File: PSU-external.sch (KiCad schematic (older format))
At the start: 40 parts, among them J3 IEC-C13-SOCKET, P18 CONN_1, P19 CONN_1, P20 CONN_1, P21 CONN_1, P22 CONN_1, T1 TRIAD-FS16-400-C2, T2 TRIAD-FS48-750-C2, U10 P0720ECL, U11 P0720ECL, U12 MC7805C, U13 LM7818CT, U14 LM7918CT

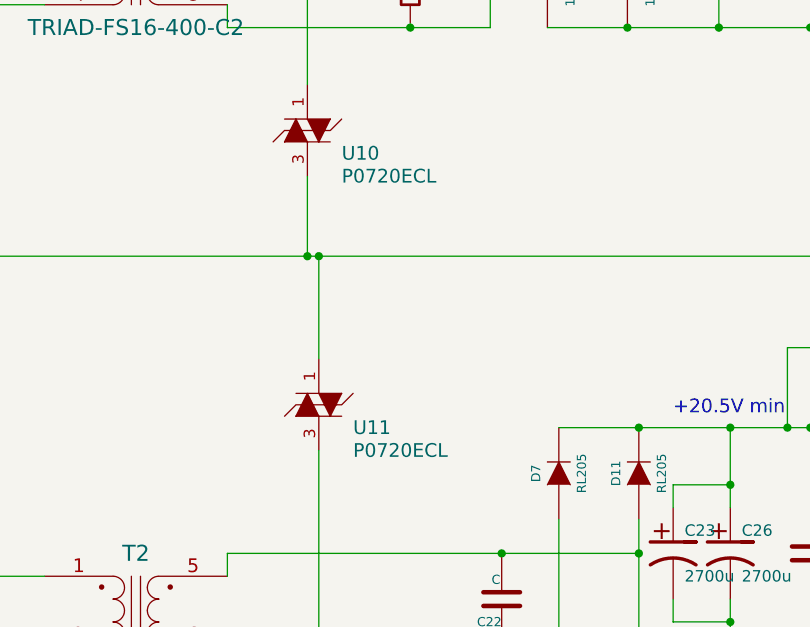
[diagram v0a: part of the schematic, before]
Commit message: Changed from the P0720ECL SIDACtor to the more sensitive P0300.
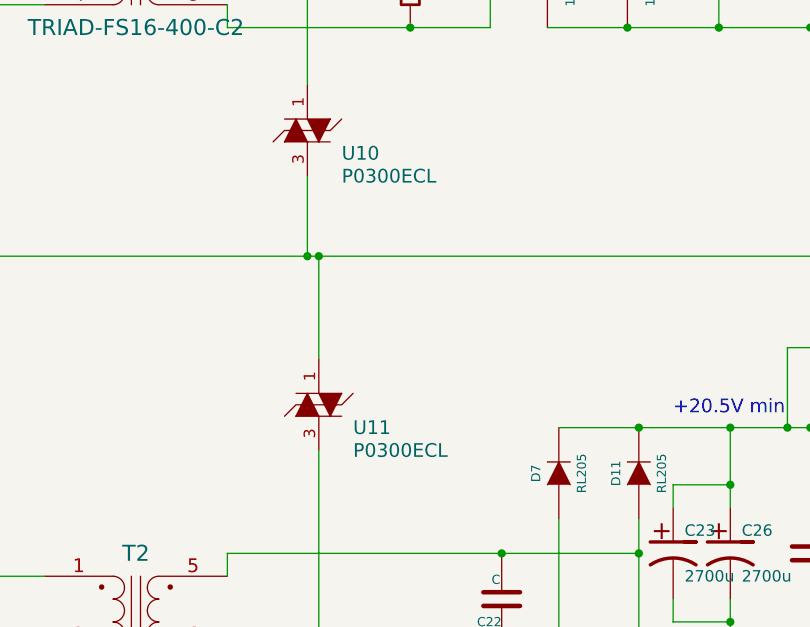
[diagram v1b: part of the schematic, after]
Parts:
- removed U10, U11: P0720ECL, symbol P0720ECL
- added U10, U11: P0300ECL, symbol P0300ECL
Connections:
- net AGND_EXT: now also U11.3
- net SAF_GND: now also U10.3, U11.1
- net at T1.6 (SB), T1.7 (SC): now also U10.1
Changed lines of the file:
@@
 Wire Wire Line
 	5400 3850 5400 4800
-$Comp
-L P0720ECL U10
-U 1 1 537CB1E3
-P 5350 2450
-F 0 "U10" H 5500 2350 60  0000 L CNN
-F 1 "P0720ECL" H 5500 2250 60  0000 L CNN
-F 2 "" H 5350 2500 60  0001 C CNN
-F 3 "~" H 5350 2500 60  0000 C CNN
-F 4 "F5278-ND" H 5350 2450 60  0001 C CNN "DigiKey"
-	1    5350 2450
-	1    0    0    -1
-$EndComp
 Wire Wire Line
 	6950 5050 6950 4950
@@
 	1    6750 1800
 	0    -1   -1   0
-$EndComp
-$Comp
-L P0720ECL U11
-U 1 1 537DAB3C
-P 5400 3650
-F 0 "U11" H 5550 3550 60  0000 L CNN
-F 1 "P0720ECL" H 5550 3450 60  0000 L CNN
-F 2 "" H 5400 3700 60  0001 C CNN
-F 3 "~" H 5400 3700 60  0000 C CNN
-F 4 "F5278-ND" H 5400 3650 60  0001 C CNN "DigiKey"
-	1    5400 3650
-	1    0    0    -1
 $EndComp
 $Comp
@@
 	2400 2900 2400 3000
 Connection ~ 2400 3000
+$Comp
+L P0300ECL U10
+U 1 1 5389743A
+P 5350 2450
+F 0 "U10" H 5500 2350 60  0000 L CNN
+F 1 "P0300ECL" H 5500 2250 60  0000 L CNN
+F 2 "" H 5350 2500 60  0000 C CNN
+F 3 "" H 5350 2500 60  0000 C CNN
+F 4 "P0300ECL-ND" H 5350 2450 60  0001 C CNN "DigiKey"
+	1    5350 2450
+	1    0    0    -1
+$EndComp
+$Comp
+L P0300ECL U11
+U 1 1 53897463
+P 5400 3650
+F 0 "U11" H 5550 3550 60  0000 L CNN
+F 1 "P0300ECL" H 5550 3450 60  0000 L CNN
+F 2 "" H 5400 3700 60  0000 C CNN
+F 3 "" H 5400 3700 60  0000 C CNN
+F 4 "P0300ECL-ND" H 5400 3650 60  0001 C CNN "DigiKey"
+	1    5400 3650
+	1    0    0    -1
+$EndComp
 $EndSCHEMATC

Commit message: Changed to use the fixed IEC socket device; the PSU netlist should now be (more) correct.
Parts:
- C21, C22: footprint (none) -> Capacitors_ThroughHole:Capacitor12MMDiscRM7.75
- F1, J3: footprint (none) -> Oddities:Dummy_Empty
- P18, P19, P20, P21, P22: footprint (none) -> Connect:1pin
- R21, R22: footprint (none) -> Resistors_ThroughHole:Resistor_Horizontal_RM15mm
- U10, U11: footprint (none) -> Housings_TO-92:TO-92-Free-inline-wide
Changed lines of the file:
@@
 F 0 "C22" H 6200 4600 40  0000 L CNN
 F 1 "C" H 6206 4415 40  0000 L CNN
-F 2 "" H 6238 4350 30  0001 C CNN
+F 2 "Capacitors_ThroughHole:Capacitor12MMDiscRM7.75" H 6238 4350 30  0001 C CNN
 F 3 "~" H 6200 4500 60  0000 C CNN
 	1    6200 4500
@@
 F 0 "R22" V 6280 5100 40  0000 C CNN
 F 1 "R" V 6207 5101 40  0000 C CNN
-F 2 "" V 6130 5100 30  0001 C CNN
+F 2 "Resistors_ThroughHole:Resistor_Horizontal_RM15mm" V 6130 5100 30  0001 C CNN
 F 3 "~" H 6200 5100 30  0000 C CNN
 	1    6200 5100
@@
 F 0 "C21" H 5800 1300 40  0000 L CNN
 F 1 "C" H 5806 1115 40  0000 L CNN
-F 2 "" H 5838 1050 30  0001 C CNN
+F 2 "Capacitors_ThroughHole:Capacitor12MMDiscRM7.75" H 5838 1050 30  0001 C CNN
 F 3 "~" H 5800 1200 60  0000 C CNN
 	1    5800 1200
@@
 F 0 "R21" V 5880 1750 40  0000 C CNN
 F 1 "R" V 5807 1751 40  0000 C CNN
-F 2 "" V 5730 1750 30  0001 C CNN
+F 2 "Resistors_ThroughHole:Resistor_Horizontal_RM15mm" V 5730 1750 30  0001 C CNN
 F 3 "~" H 5800 1750 30  0000 C CNN
 	1    5800 1750
@@
 F 0 "J3" H 1800 3000 60  0000 L CNN
 F 1 "IEC-C13-SOCKET" H 1800 2900 60  0000 L CNN
-F 2 "" H 2000 4100 60  0001 C CNN
+F 2 "Oddities:Dummy_Empty" H 2000 4100 60  0001 C CNN
 F 3 "~" H 2000 4100 60  0000 C CNN
 F 4 "CCM1724-ND" H 2050 3700 60  0001 C CNN "DigiKey"
@@
 F 0 "F1" H 2650 5050 40  0000 C CNN
 F 1 "FUSE" H 2450 4950 40  0000 C CNN
-F 2 "" H 2550 5000 60  0001 C CNN
+F 2 "Oddities:Dummy_Empty" H 2550 5000 60  0001 C CNN
 F 3 "~" H 2550 5000 60  0000 C CNN
 F 4 "F1764-ND" H 2550 5000 60  0001 C CNN "DigiKey"
@@
 F 0 "P22" H 3080 3700 40  0000 L CNN
 F 1 "CONN_1" H 3000 3755 30  0001 C CNN
-F 2 "" H 3000 3700 60  0000 C CNN
+F 2 "Connect:1pin" H 3000 3700 60  0001 C CNN
 F 3 "" H 3000 3700 60  0000 C CNN
 	1    3000 3700
@@
 F 0 "P21" H 2930 3700 40  0000 L CNN
 F 1 "CONN_1" H 2850 3755 30  0001 C CNN
-F 2 "" H 2850 3700 60  0000 C CNN
+F 2 "Connect:1pin" H 2850 3700 60  0001 C CNN
 F 3 "" H 2850 3700 60  0000 C CNN
 	1    2850 3700
@@
 F 0 "P20" H 2780 3700 40  0000 L CNN
 F 1 "CONN_1" H 2700 3755 30  0001 C CNN
-F 2 "" H 2700 3700 60  0000 C CNN
+F 2 "Connect:1pin" H 2700 3700 60  0001 C CNN
 F 3 "" H 2700 3700 60  0000 C CNN
 	1    2700 3700
@@
 F 0 "P19" H 2630 3700 40  0000 L CNN
 F 1 "CONN_1" H 2550 3755 30  0001 C CNN
-F 2 "" H 2550 3700 60  0000 C CNN
+F 2 "Connect:1pin" H 2550 3700 60  0001 C CNN
 F 3 "" H 2550 3700 60  0000 C CNN
 	1    2550 3700
@@
 F 0 "P18" H 2480 2750 40  0000 L CNN
 F 1 "CONN_1" H 2400 2805 30  0001 C CNN
-F 2 "" H 2400 2750 60  0000 C CNN
+F 2 "Connect:1pin" H 2400 2750 60  0001 C CNN
 F 3 "" H 2400 2750 60  0000 C CNN
 	1    2400 2750
@@
 F 0 "U10" H 5500 2350 60  0000 L CNN
 F 1 "P0300ECL" H 5500 2250 60  0000 L CNN
-F 2 "" H 5350 2500 60  0000 C CNN
+F 2 "Housings_TO-92:TO-92-Free-inline-wide" H 5350 2500 60  0001 C CNN
 F 3 "" H 5350 2500 60  0000 C CNN
 F 4 "P0300ECL-ND" H 5350 2450 60  0001 C CNN "DigiKey"
@@
 F 0 "U11" H 5550 3550 60  0000 L CNN
 F 1 "P0300ECL" H 5550 3450 60  0000 L CNN
-F 2 "" H 5400 3700 60  0000 C CNN
+F 2 "Housings_TO-92:TO-92-Free-inline-wide" H 5400 3700 60  0001 C CNN
 F 3 "" H 5400 3700 60  0000 C CNN
 F 4 "P0300ECL-ND" H 5400 3650 60  0001 C CNN "DigiKey"

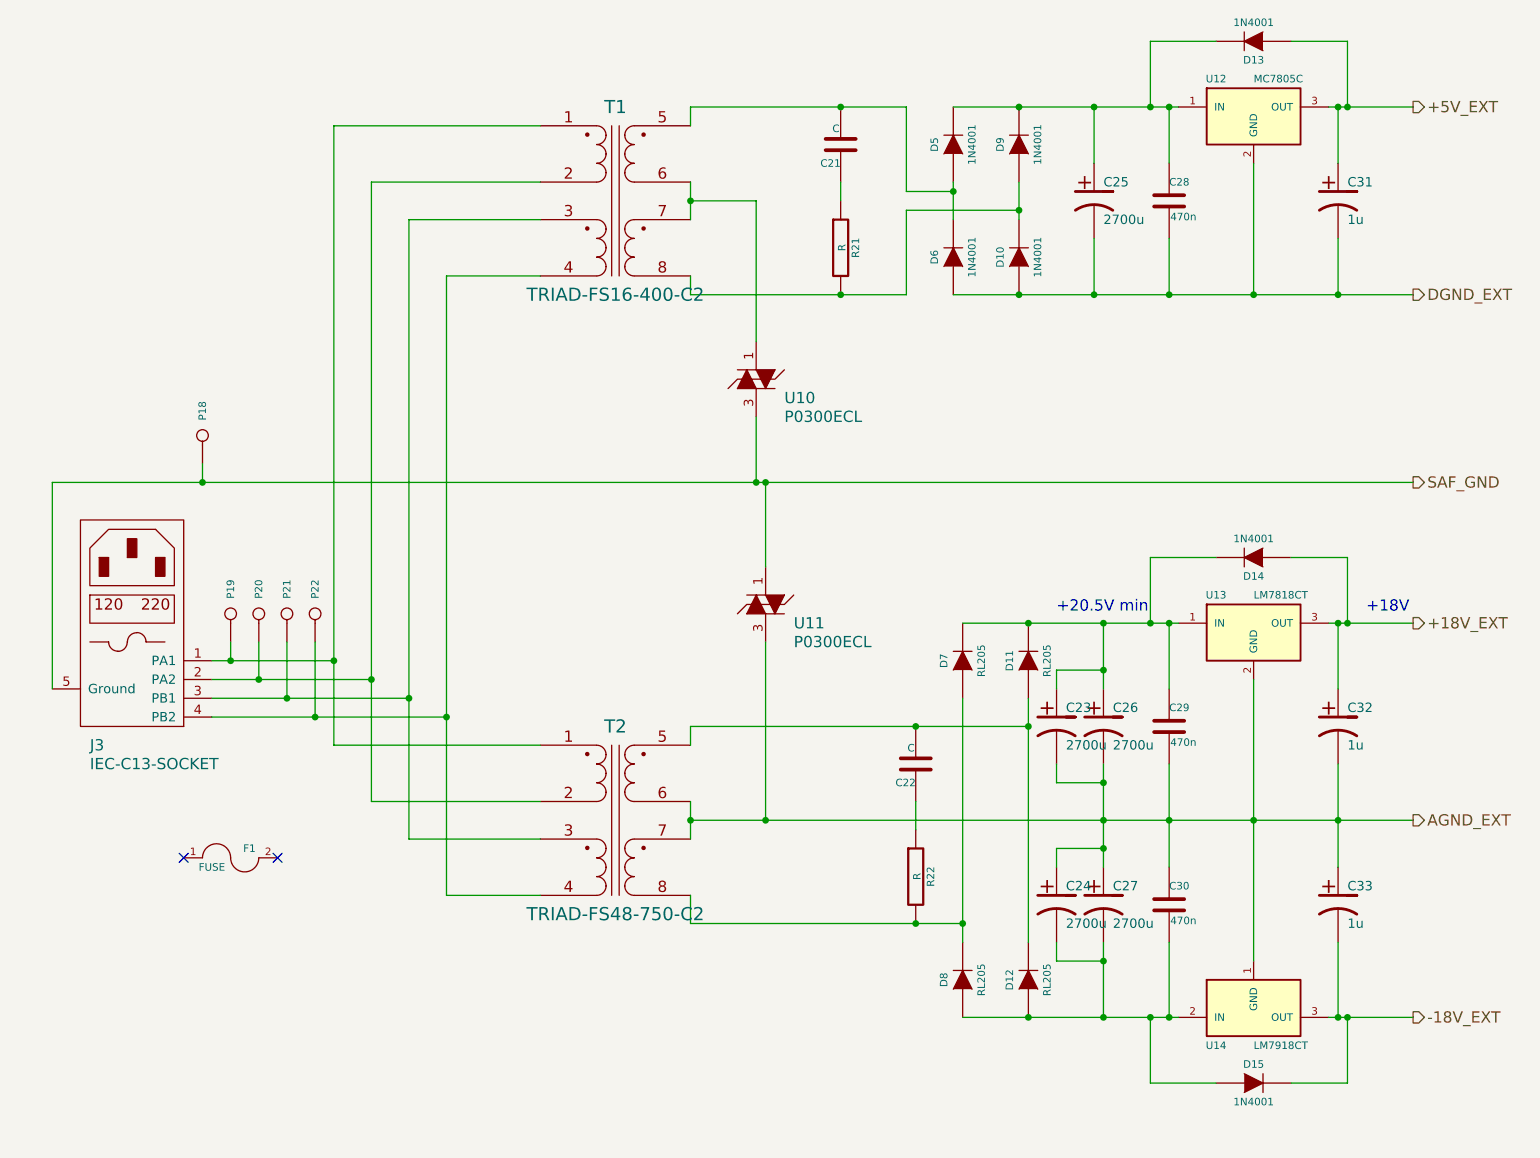
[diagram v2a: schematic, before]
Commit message: A lot of routing, some parts changes:   * Added snubber C/RC snubbers to transformer secondaries.   * Changed PSU OA from OPA209 to OPA27.   * Routed external PSU.   * Mostly done routing internal circuits.  Just need to get everything together.   * Changed digital transformer to a more appropriately-specced one.
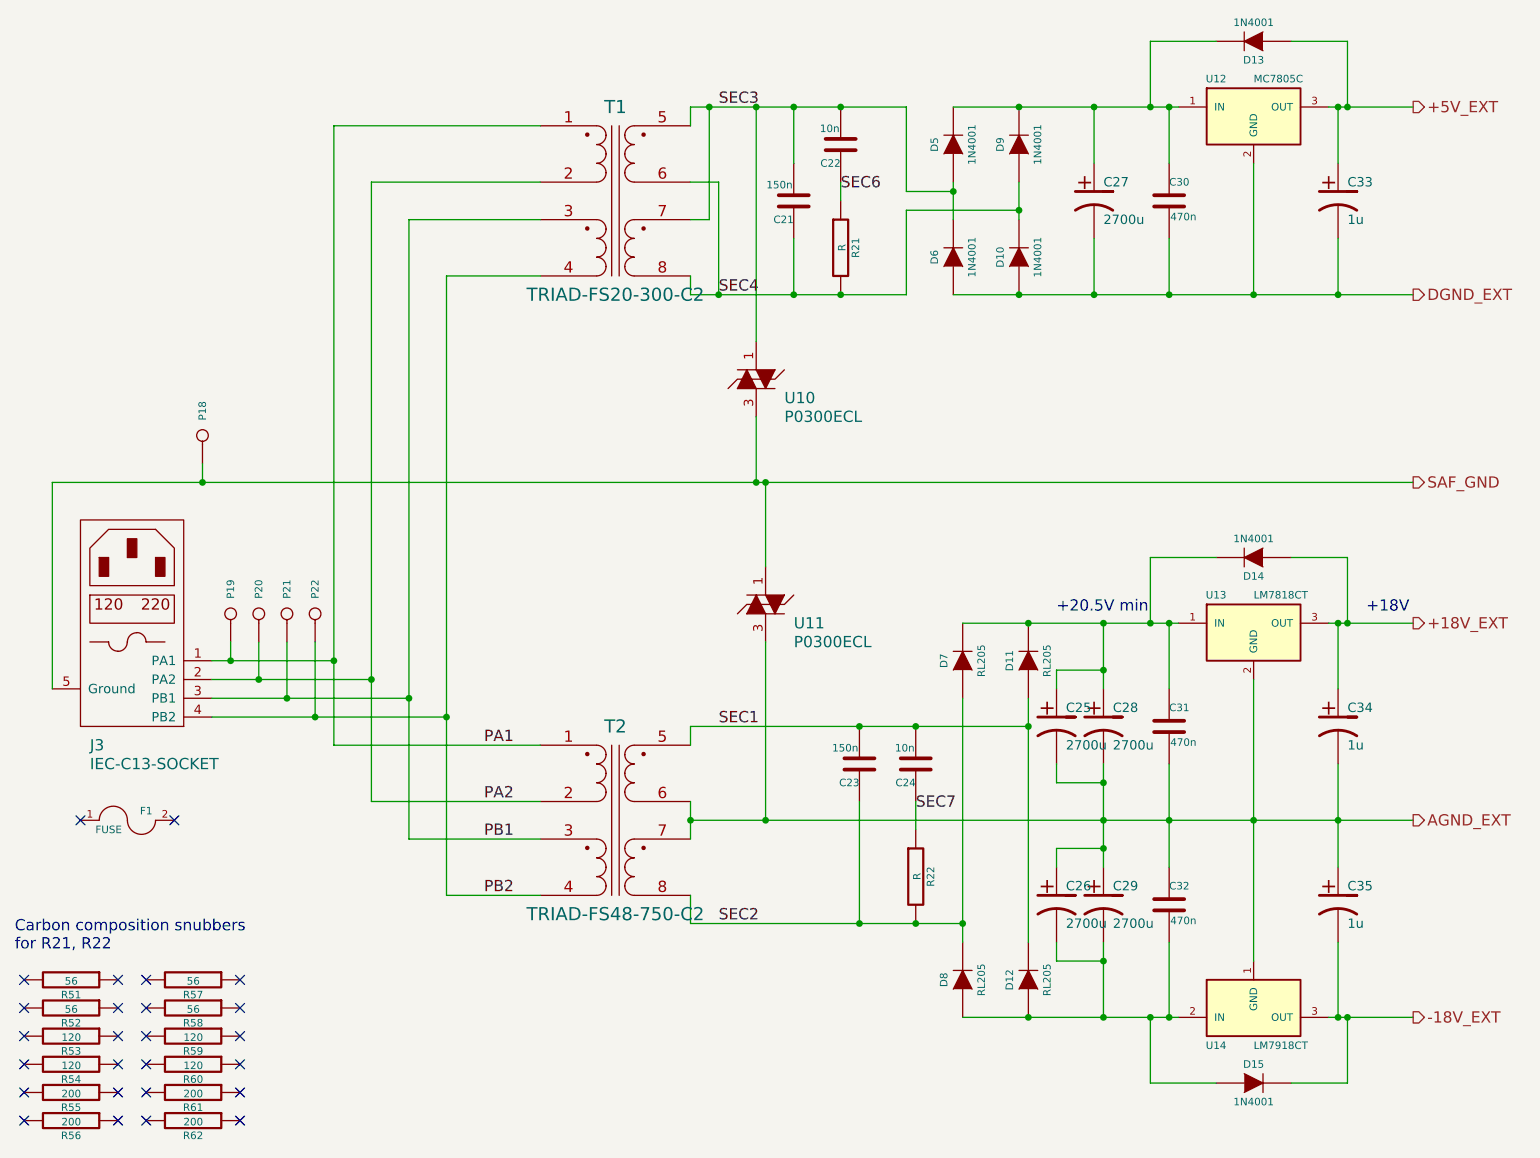
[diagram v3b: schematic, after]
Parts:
- removed T1: TRIAD-FS16-400-C2, my-trafos:TRIAD_FS16_400_C2, symbol TRIAD-FS16-400-C2
- added C21, C23: 150n, Capacitors_ThroughHole:Capacitor18x6RM15, symbol C
- added R51, R52, R57, R58: 56, symbol R
- added R53, R54, R59, R60: 120, symbol R
- added R55, R56, R61, R62: 200, symbol R
- added T1: TRIAD-FS20-300-C2, my-trafos:TRIAD_FS16_400_C2, symbol TRIAD-FS20-300-C2
- C22: renamed from C21; value C -> 10n; footprint Capacitors_ThroughHole:Capacitor12MMDiscRM7.75 -> Capacitors_ThroughHole:Capacitor13x4RM10; DigiKey (none) -> 399-5986-ND
- C24: renamed from C22; value C -> 10n; footprint Capacitors_ThroughHole:Capacitor12MMDiscRM7.75 -> Capacitors_ThroughHole:Capacitor13x4RM10; DigiKey (none) -> 399-5986-ND
- renumbered C23 to C25, C24 to C26, C25 to C27, C26 to C28, C27 to C29, C28 to C30, C29 to C31, C30 to C32, C31 to C33, C32 to C34, C33 to C35
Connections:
- net SEC3: now reaches C22.2, D5.1 (A), D6.2 (K)
- net SEC3: now also U10.1, C21.2, T1.5 (SA), T1.7 (SC)
- net SEC2: now reaches D7.1 (A), D8.2 (K), R22.2, T2.8 (SD)
- net SEC2: now also C23.1
- net SEC7: now reaches C24.1, R22.1
- net SEC1: now reaches C24.2, D11.1 (A), D12.2 (K), T2.5 (SA)
- net SEC1: now also C23.2
- net SEC6: now reaches C22.1, R21.1
- net SEC4: now reaches D10.2 (K), D9.1 (A), R21.2
- net SEC4: now also C21.1, T1.6 (SB), T1.8 (SD)
- net PA1: now reaches J3.1 (PA1), P19.1, T2.1 (AA)
- net PA1: now also T1.1 (AA)
- net PA2: now reaches J3.2 (PA2), P20.1, T2.2 (AB)
- net PA2: now also T1.2 (AB)
- net PB1: now reaches J3.3 (PB1), P21.1, T2.3 (AC)
- net PB1: now also T1.3 (AC)
- net PB2: now reaches J3.4 (PB2), P22.1, T2.4 (AD)
- net PB2: now also T1.4 (AD)
- no-connect marks 2 -> 26
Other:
- note added: "Carbon composition snubbers\nfor R21, R22"
- moved on the sheet: F1
